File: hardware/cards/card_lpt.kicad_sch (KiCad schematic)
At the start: 20 parts, among them J1 DB25_Pins, U1 74HCT374, U10 74HCT32, U11 74HCT32, U2 74HCT374, U3 74HCT244, U4 74HCT245, U5 74HCT244, U6 74HCT138, U7 74HCT08, U8 74HCT08, U9 74HCT04

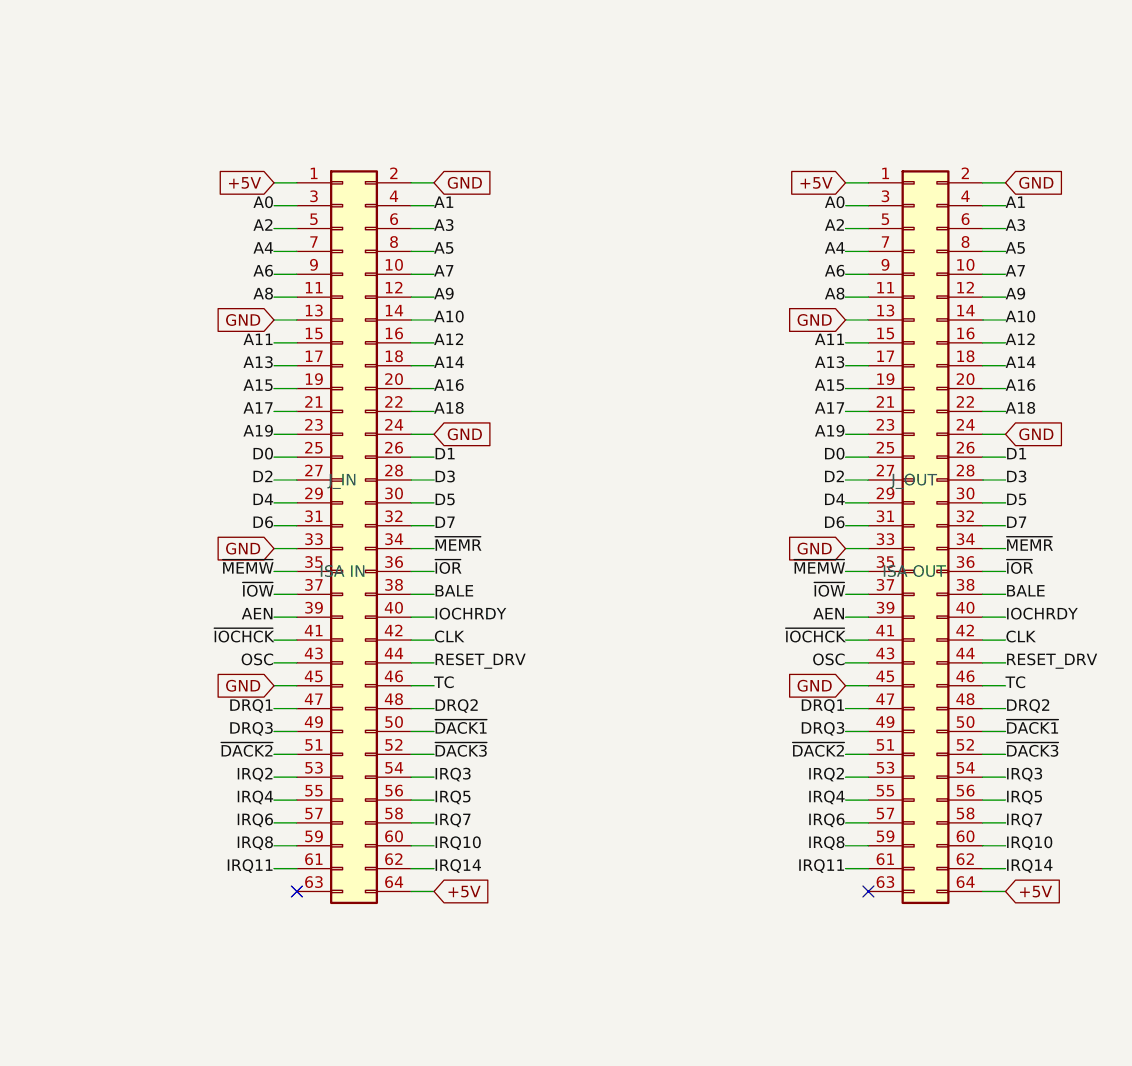
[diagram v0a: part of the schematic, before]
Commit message: Re-base ISA connector on standard 8-bit ISA pinout (60-pin, PicoGUS-style)
isa_conn now uses the standard 8-bit ISA edge pinout on a 60-pin 2.54mm header
(Conn_02x30_Odd_Even), matching the PicoGUS Bus_ISA_8bit layout so the sidecar and
dev cards are pin-compatible with real ISA cards (and 60-pin ribbon is easy to
source). The unused ISA analog rails are reclaimed: pin7 -5V->~{IOCHCK}, pin11
-12V->GND (extra return), pin15 +12V->IRQ8; pin13 reserved/0WS# left NC. Drops the
non-standard IRQ10/11/14 (16-bit-extension signals on a real AT); DACK0/REFRESH#
now on its standard pin (undriven, for card compatibility). Change is confined to
isa_conn.py; sidecar + all card_* sheets inherit it. Verified pin map and
connectivity (IOCHCK->Bus MCU, IRQ8->collector+RTC); zero structural ERC on
motherboard and all five cards.

Co-Authored-By: Claude Opus 4.8 (1M context) <noreply@anthropic.com>
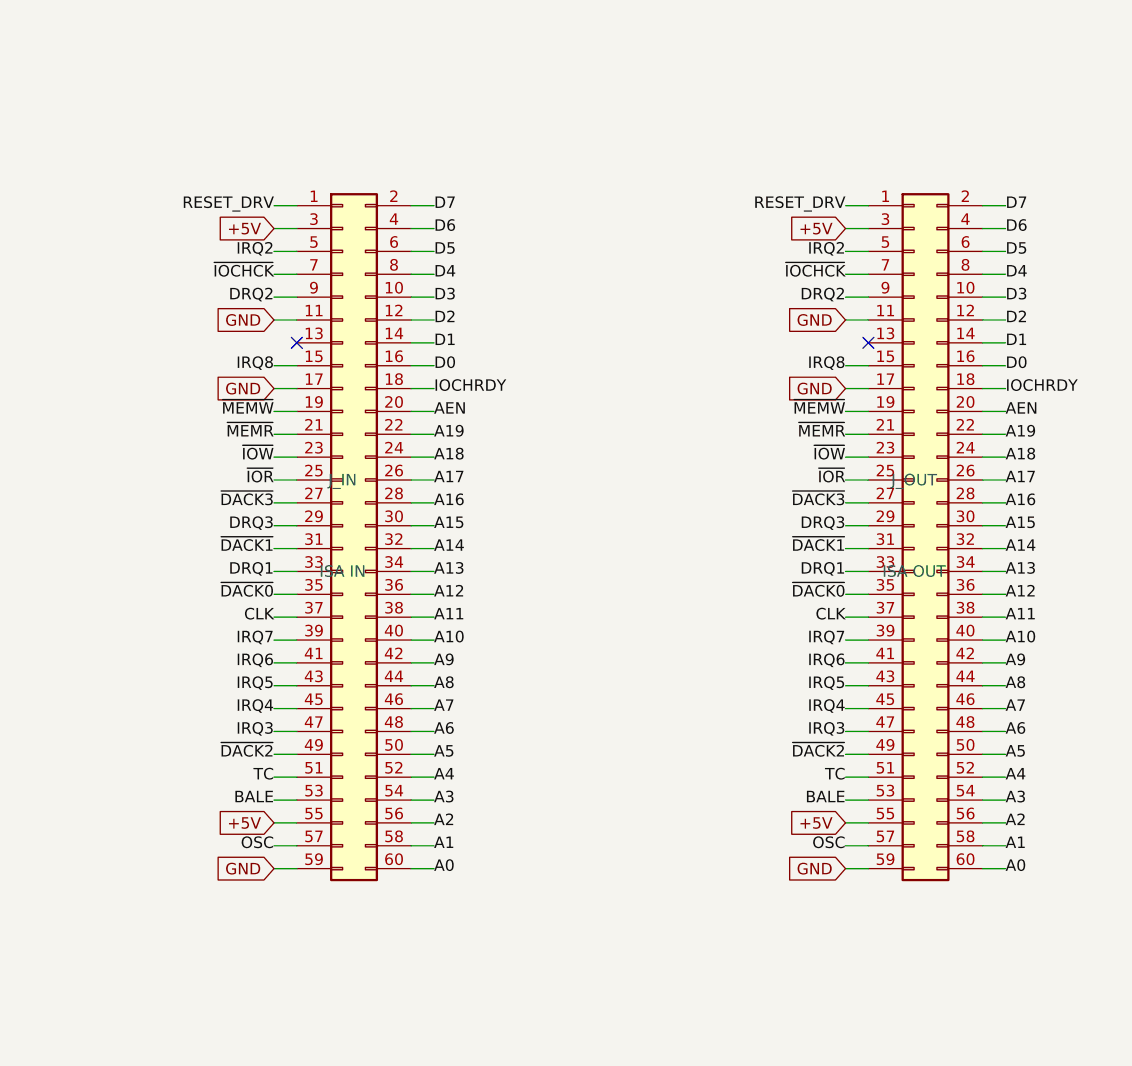
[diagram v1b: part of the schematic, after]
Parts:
- removed J_IN: ISA IN, symbol Connector_Generic:Conn_02x32_Odd_Even
- removed J_OUT: ISA OUT, symbol Connector_Generic:Conn_02x32_Odd_Even
- added J_IN: ISA IN, symbol Connector_Generic:Conn_02x30_Odd_Even
- added J_OUT: ISA OUT, symbol Connector_Generic:Conn_02x30_Odd_Even
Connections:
- net +5V: now also J_IN.3 (Pin_3), J_IN.55 (Pin_55), J_OUT.3 (Pin_3), J_OUT.55 (Pin_55)
- net A0: now also J_IN.60 (Pin_60), J_OUT.60 (Pin_60)
- net A1: now also J_IN.58 (Pin_58), J_OUT.58 (Pin_58)
- net A10: now also J_IN.40 (Pin_40), J_OUT.40 (Pin_40)
- net A11: now also J_IN.38 (Pin_38), J_OUT.38 (Pin_38)
- net A12: now also J_IN.36 (Pin_36), J_OUT.36 (Pin_36)
- net A13: now also J_IN.34 (Pin_34), J_OUT.34 (Pin_34)
- net A14: now also J_IN.32 (Pin_32), J_OUT.32 (Pin_32)
- net A15: now also J_IN.30 (Pin_30), J_OUT.30 (Pin_30)
- net A16: now also J_IN.28 (Pin_28), J_OUT.28 (Pin_28)
- net A17: now also J_IN.26 (Pin_26), J_OUT.26 (Pin_26)
- net A18: now also J_IN.24 (Pin_24), J_OUT.24 (Pin_24)
- net A19: now also J_IN.22 (Pin_22), J_OUT.22 (Pin_22)
- net A2: now also J_IN.56 (Pin_56), J_OUT.56 (Pin_56)
- net A3: now also J_IN.54 (Pin_54), J_OUT.54 (Pin_54)
- net A4: now also J_IN.52 (Pin_52), J_OUT.52 (Pin_52)
- net A5: now also J_IN.50 (Pin_50), J_OUT.50 (Pin_50)
- net A6: now also J_IN.48 (Pin_48), J_OUT.48 (Pin_48)
- net A7: now also J_IN.46 (Pin_46), J_OUT.46 (Pin_46)
- net A8: now also J_IN.44 (Pin_44), J_OUT.44 (Pin_44)
- net A9: now also J_IN.42 (Pin_42), J_OUT.42 (Pin_42)
- net AEN: now also J_IN.20 (Pin_20), J_OUT.20 (Pin_20)
- net BALE: now also J_IN.53 (Pin_53), J_OUT.53 (Pin_53)
- net CLK: now also J_IN.37 (Pin_37), J_OUT.37 (Pin_37)
- net D0: now also J_IN.16 (Pin_16), J_OUT.16 (Pin_16)
- net D1: now also J_IN.14 (Pin_14), J_OUT.14 (Pin_14)
- net D2: now also J_IN.12 (Pin_12), J_OUT.12 (Pin_12)
- net D3: now also J_IN.10 (Pin_10), J_OUT.10 (Pin_10)
- net D4: now also J_IN.8 (Pin_8), J_OUT.8 (Pin_8)
- net D5: now also J_IN.6 (Pin_6), J_OUT.6 (Pin_6)
- net D6: now also J_IN.4 (Pin_4), J_OUT.4 (Pin_4)
- net D7: now also J_IN.2 (Pin_2), J_OUT.2 (Pin_2)
- net DRQ1: now also J_IN.33 (Pin_33), J_OUT.33 (Pin_33)
- net DRQ2: now also J_IN.9 (Pin_9), J_OUT.9 (Pin_9)
- net DRQ3: now also J_IN.29 (Pin_29), J_OUT.29 (Pin_29)
- net GND: now also J_IN.11 (Pin_11), J_IN.17 (Pin_17), J_IN.59 (Pin_59), J_OUT.11 (Pin_11), J_OUT.17 (Pin_17), J_OUT.59 (Pin_59)
- net IOCHRDY: now also J_IN.18 (Pin_18), J_OUT.18 (Pin_18)
- net IRQ2: now also J_IN.5 (Pin_5), J_OUT.5 (Pin_5)
- net IRQ3: now also J_IN.47 (Pin_47), J_OUT.47 (Pin_47)
- net IRQ4: now also J_IN.45 (Pin_45), J_OUT.45 (Pin_45)
- net IRQ5: now also J_IN.43 (Pin_43), J_OUT.43 (Pin_43)
- net IRQ6: now also J_IN.41 (Pin_41), J_OUT.41 (Pin_41)
- net IRQ7: now also J_IN.39 (Pin_39), J_OUT.39 (Pin_39)
- net IRQ8: now also J_IN.15 (Pin_15), J_OUT.15 (Pin_15)
- net OSC: now also J_IN.57 (Pin_57), J_OUT.57 (Pin_57)
- net RESET_DRV: now also J_IN.1 (Pin_1), J_OUT.1 (Pin_1)
- net TC: now also J_IN.51 (Pin_51), J_OUT.51 (Pin_51)
- net ~{DACK1}: now also J_IN.31 (Pin_31), J_OUT.31 (Pin_31)
- net ~{DACK2}: now also J_IN.49 (Pin_49), J_OUT.49 (Pin_49)
- net ~{DACK3}: now also J_IN.27 (Pin_27), J_OUT.27 (Pin_27)
- net ~{IOCHCK}: now also J_IN.7 (Pin_7), J_OUT.7 (Pin_7)
- net ~{IOR}: now also J_IN.25 (Pin_25), J_OUT.25 (Pin_25)
- net ~{IOW}: now also J_IN.23 (Pin_23), J_OUT.23 (Pin_23)
- net ~{MEMR}: now also J_IN.21 (Pin_21), J_OUT.21 (Pin_21)
- net ~{MEMW}: now also J_IN.19 (Pin_19), J_OUT.19 (Pin_19)
- new net ~{DACK0}: J_IN.35 (Pin_35), J_OUT.35 (Pin_35)

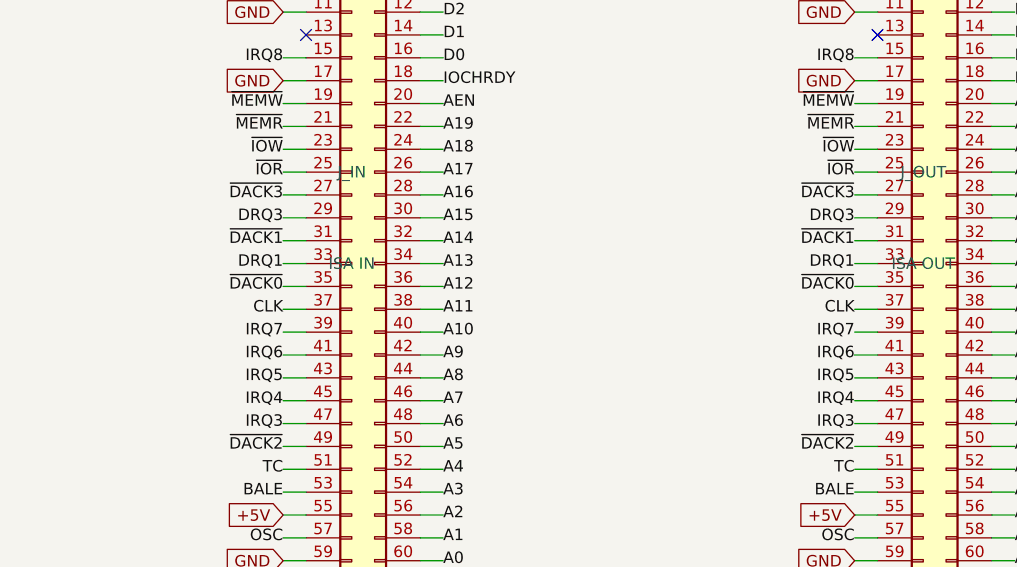
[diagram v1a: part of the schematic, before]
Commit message: Drive ISA REFRESH# from the Bus MCU for DRAM-based cards
Pin 35 (DACK0/REFRESH#) net renamed ~{DACK0} -> ~{REFRESH} in isa_conn and is now
an active Bus MCU output (GPIO47, reclaimed from the redundant raw-~WR sense -- the
MCU tracks writes via the gated MEMW/IOW). Driven from the internal ~15us refresh
timer (same source as the 0x61-bit-4 toggle); a refresh cycle reuses the bus-master
engine to walk the row address on A0-A7 + pulse MEMR#, so DRAM ISA cards see a
standard refresh. ~{REFRESH} added to the Bus MCU interface. Verified it ties
sidecar<->Bus MCU and passes through J_IN<->J_OUT on every dev card; zero
structural ERC on motherboard and all five cards.

Co-Authored-By: Claude Opus 4.8 (1M context) <noreply@anthropic.com>
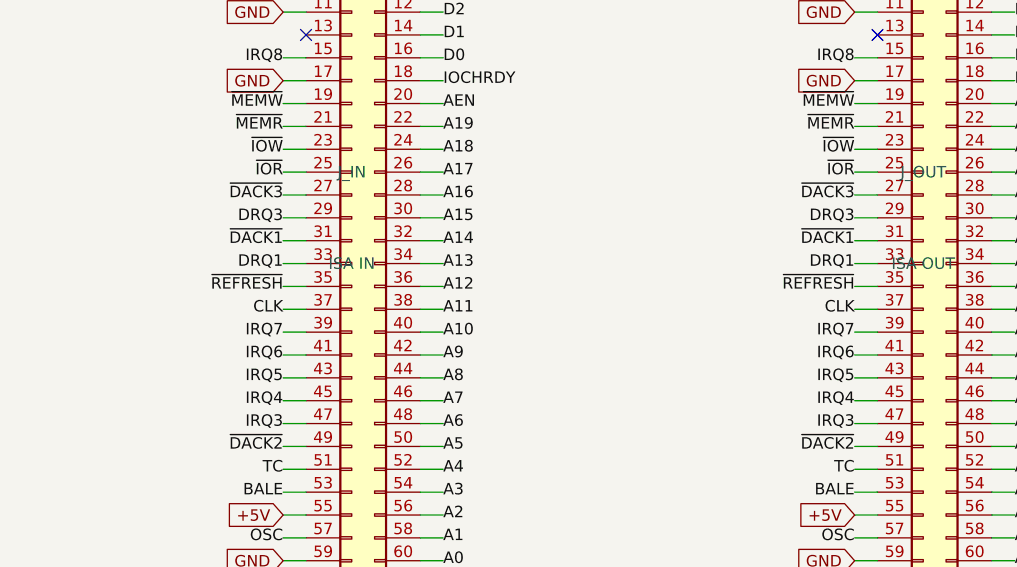
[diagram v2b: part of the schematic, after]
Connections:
- net ~{DACK0} renamed ~{REFRESH}
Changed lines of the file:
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@@
 		)
 	)
-	(label "~{DACK0}"
+	(label "~{REFRESH}"
 		(at 436.88 160.02 180)
 		(effects
@@
 		)
 	)
-	(label "~{DACK0}"
+	(label "~{REFRESH}"
 		(at 500.38 160.02 180)
 		(effects
@@
 		(instances
 			(project "card_lpt"
-				(path "/6a3e43c0-a07d-481b-9625-a33615572297"
+				(path "/3601480a-62b4-4d7d-acc2-271a667b1cb5"
 					(reference "J_IN")
 					(unit 1)
@@
 		(instances
 			(project "card_lpt"
-				(path "/6a3e43c0-a07d-481b-9625-a33615572297"
+				(path "/3601480a-62b4-4d7d-acc2-271a667b1cb5"
 					(reference "J_OUT")
 					(unit 1)
@@
 		(instances
 			(project "card_lpt"
-				(path "/6a3e43c0-a07d-481b-9625-a33615572297"
+				(path "/3601480a-62b4-4d7d-acc2-271a667b1cb5"
 					(reference "U7")
 					(unit 1)
@@
 		(instances
 			(project "card_lpt"
-				(path "/6a3e43c0-a07d-481b-9625-a33615572297"
+				(path "/3601480a-62b4-4d7d-acc2-271a667b1cb5"
 					(reference "U8")
 					(unit 1)
@@
 		(instances
 			(project "card_lpt"
-				(path "/6a3e43c0-a07d-481b-9625-a33615572297"
+				(path "/3601480a-62b4-4d7d-acc2-271a667b1cb5"
 					(reference "U9")
 					(unit 1)
@@
 		(instances
 			(project "card_lpt"
-				(path "/6a3e43c0-a07d-481b-9625-a33615572297"
+				(path "/3601480a-62b4-4d7d-acc2-271a667b1cb5"
 					(reference "U6")
 					(unit 1)
@@
 		(instances
 			(project "card_lpt"
-				(path "/6a3e43c0-a07d-481b-9625-a33615572297"
+				(path "/3601480a-62b4-4d7d-acc2-271a667b1cb5"
 					(reference "U10")
 					(unit 1)
@@
 		(instances
 			(project "card_lpt"
-				(path "/6a3e43c0-a07d-481b-9625-a33615572297"
+				(path "/3601480a-62b4-4d7d-acc2-271a667b1cb5"
 					(reference "U11")
 					(unit 1)
@@
 		(instances
 			(project "card_lpt"
-				(path "/6a3e43c0-a07d-481b-9625-a33615572297"
+				(path "/3601480a-62b4-4d7d-acc2-271a667b1cb5"
 					(reference "U1")
 					(unit 1)
@@
 		(instances
 			(project "card_lpt"
-				(path "/6a3e43c0-a07d-481b-9625-a33615572297"
+				(path "/3601480a-62b4-4d7d-acc2-271a667b1cb5"
 					(reference "U4")
 					(unit 1)
@@
 		(instances
 			(project "card_lpt"
-				(path "/6a3e43c0-a07d-481b-9625-a33615572297"
+				(path "/3601480a-62b4-4d7d-acc2-271a667b1cb5"
 					(reference "U2")
 					(unit 1)
@@
 		(instances
 			(project "card_lpt"
-				(path "/6a3e43c0-a07d-481b-9625-a33615572297"
+				(path "/3601480a-62b4-4d7d-acc2-271a667b1cb5"
 					(reference "U5")
 					(unit 1)
@@
 		(instances
 			(project "card_lpt"
-				(path "/6a3e43c0-a07d-481b-9625-a33615572297"
+				(path "/3601480a-62b4-4d7d-acc2-271a667b1cb5"
 					(reference "U3")
 					(unit 1)
@@
 		(instances
 			(project "card_lpt"
-				(path "/6a3e43c0-a07d-481b-9625-a33615572297"
+				(path "/3601480a-62b4-4d7d-acc2-271a667b1cb5"
 					(reference "J1")
 					(unit 1)
@@
 		(instances
 			(project "card_lpt"
-				(path "/6a3e43c0-a07d-481b-9625-a33615572297"
+				(path "/3601480a-62b4-4d7d-acc2-271a667b1cb5"
 					(reference "C1")
 					(unit 1)
@@
 		(instances
 			(project "card_lpt"
-				(path "/6a3e43c0-a07d-481b-9625-a33615572297"
+				(path "/3601480a-62b4-4d7d-acc2-271a667b1cb5"
 					(reference "C2")
 					(unit 1)
@@
 		(instances
 			(project "card_lpt"
-				(path "/6a3e43c0-a07d-481b-9625-a33615572297"
+				(path "/3601480a-62b4-4d7d-acc2-271a667b1cb5"
 					(reference "C3")
 					(unit 1)
@@
 		(instances
 			(project "card_lpt"
-				(path "/6a3e43c0-a07d-481b-9625-a33615572297"
+				(path "/3601480a-62b4-4d7d-acc2-271a667b1cb5"
 					(reference "C4")
 					(unit 1)
@@
 		(instances
 			(project "card_lpt"
-				(path "/6a3e43c0-a07d-481b-9625-a33615572297"
+				(path "/3601480a-62b4-4d7d-acc2-271a667b1cb5"
 					(reference "C5")
 					(unit 1)
@@
 		(instances
 			(project "card_lpt"
-				(path "/6a3e43c0-a07d-481b-9625-a33615572297"
+				(path "/3601480a-62b4-4d7d-acc2-271a667b1cb5"
 					(reference "C6")
 					(unit 1)

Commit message: Fix all critical+high design-review findings (C1-C5, H1-H8)
Full review in hardware/notes/design-review-2026-07-03.md (with per-item
fix logs). Highlights:
- SRAM strobed by gated MEMR/MEMW (was raw ~RD/~WR: I/O cycles corrupted
  SRAM and the boot shadow-load could never write it)
- Reset chain implemented: NAND combine of ~PWRGOOD + ~CPURESET drives
  V20 RESET and an always-driven RESET_DRV (dropped from the Bus MCU)
- Contention-free bus handoff: '573 OE=HLDA vs counter '244 stage
  ~OE=~HLDA; strobe gates wired + tri-stated ('125, ~OE=HLDA); Bus MCU
  address group fixed to sense; AEN/TC fixed drive; BALE input-only
- '573 LE driven by BALE (was a dangling BALE_L label)
- Data '245 DIR=DT/~R, ~OE=DEN so INTA vectors reach the CPU
- Idle pulls: strobes/DEN high, AEN/IRQ2-9/DRQ low, IOCHRDY/IOCHCK/
  DACK2-3 high
- CH224K CFG1 left open (grounding it selects 9-20V, not 5V)
- XT-IDE INTRQ pull-down (pull-up parked IRQ5 asserted)
- LPT status bit7 = ~Busy via spare inverter (SPP semantics)
- Audio summer TL072 -> MCP6002 (RRIO; TL072 out of spec at +5V single
  supply)
- card_isatest: DUT P-FET gate to V5RAW + NPN driver (default off, can
  fully turn off); /3 divider TC->~PE reload actually wired

Overturned picks corrected in notes/questions-*.md. All sheets + cards
rebuilt; structural ERC = 0; fixes netlist-verified.

Co-Authored-By: Claude Fable 5 <noreply@anthropic.com>
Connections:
- net GND: no longer U9.13 (P13)
- net P_BUSY: now also U9.13 (P13); no longer U3.2 (1A0)
- net BUSY_N: now reaches U9.12 (P12)
- net BUSY_N: now also U3.2 (1A0)
- no-connect marks 18 -> 17
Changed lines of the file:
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@@
 		)
 	)
-	(global_label "GND"
-		(shape input)
+	(label "P_BUSY"
 		(at 59.69 184.15 180)
 		(effects
@@
 		)
 	)
-	(no_connect
-		(at 90.17 184.15)
+	(wire
+		(pts
+			(xy 90.17 184.15)
+			(xy 92.71 184.15)
+		)
+		(stroke
+			(width 0)
+			(type default)
+		)
+	)
+	(label "BUSY_N"
+		(at 92.71 184.15 0)
+		(effects
+			(font
+				(size 1.27 1.27)
+			)
+		)
 	)
 	(wire
@@
 		)
 	)
-	(label "P_BUSY"
+	(label "BUSY_N"
 		(at 186.69 217.17 180)
 		(effects
@@
 		(instances
 			(project "card_lpt"
-				(path "/d0d6c778-9dee-4e65-88c1-90d9ddd9256b"
+				(path "/4e3f5f18-a6f2-4a5e-a60d-ceab254b2380"
 					(reference "J_IN")
 					(unit 1)
@@
 		(instances
 			(project "card_lpt"
-				(path "/d0d6c778-9dee-4e65-88c1-90d9ddd9256b"
+				(path "/4e3f5f18-a6f2-4a5e-a60d-ceab254b2380"
 					(reference "J_OUT")
 					(unit 1)
@@
 		(instances
 			(project "card_lpt"
-				(path "/d0d6c778-9dee-4e65-88c1-90d9ddd9256b"
+				(path "/4e3f5f18-a6f2-4a5e-a60d-ceab254b2380"
 					(reference "U7")
 					(unit 1)
@@
 		(instances
 			(project "card_lpt"
-				(path "/d0d6c778-9dee-4e65-88c1-90d9ddd9256b"
+				(path "/4e3f5f18-a6f2-4a5e-a60d-ceab254b2380"
 					(reference "U8")
 					(unit 1)
@@
 		(instances
 			(project "card_lpt"
-				(path "/d0d6c778-9dee-4e65-88c1-90d9ddd9256b"
+				(path "/4e3f5f18-a6f2-4a5e-a60d-ceab254b2380"
 					(reference "U9")
 					(unit 1)
@@
 		(instances
 			(project "card_lpt"
-				(path "/d0d6c778-9dee-4e65-88c1-90d9ddd9256b"
+				(path "/4e3f5f18-a6f2-4a5e-a60d-ceab254b2380"
 					(reference "U6")
 					(unit 1)
@@
 		(instances
 			(project "card_lpt"
-				(path "/d0d6c778-9dee-4e65-88c1-90d9ddd9256b"
+				(path "/4e3f5f18-a6f2-4a5e-a60d-ceab254b2380"
 					(reference "U10")
 					(unit 1)
@@
 		(instances
 			(project "card_lpt"
-				(path "/d0d6c778-9dee-4e65-88c1-90d9ddd9256b"
+				(path "/4e3f5f18-a6f2-4a5e-a60d-ceab254b2380"
 					(reference "U11")
 					(unit 1)
@@
 		(instances
 			(project "card_lpt"
-				(path "/d0d6c778-9dee-4e65-88c1-90d9ddd9256b"
+				(path "/4e3f5f18-a6f2-4a5e-a60d-ceab254b2380"
 					(reference "U1")
 					(unit 1)
@@
 		(instances
 			(project "card_lpt"
-				(path "/d0d6c778-9dee-4e65-88c1-90d9ddd9256b"
+				(path "/4e3f5f18-a6f2-4a5e-a60d-ceab254b2380"
 					(reference "U4")
 					(unit 1)
@@
 		(instances
 			(project "card_lpt"
-				(path "/d0d6c778-9dee-4e65-88c1-90d9ddd9256b"
+				(path "/4e3f5f18-a6f2-4a5e-a60d-ceab254b2380"
 					(reference "U2")
 					(unit 1)
@@
 		(instances
 			(project "card_lpt"
-				(path "/d0d6c778-9dee-4e65-88c1-90d9ddd9256b"
+				(path "/4e3f5f18-a6f2-4a5e-a60d-ceab254b2380"
 					(reference "U5")
 					(unit 1)
@@
 		(instances
 			(project "card_lpt"
-				(path "/d0d6c778-9dee-4e65-88c1-90d9ddd9256b"
+				(path "/4e3f5f18-a6f2-4a5e-a60d-ceab254b2380"
 					(reference "U3")
 					(unit 1)
@@
 		(instances
 			(project "card_lpt"
-				(path "/d0d6c778-9dee-4e65-88c1-90d9ddd9256b"
+				(path "/4e3f5f18-a6f2-4a5e-a60d-ceab254b2380"
 					(reference "J1")
 					(unit 1)
@@
 		(instances
 			(project "card_lpt"
-				(path "/d0d6c778-9dee-4e65-88c1-90d9ddd9256b"
+				(path "/4e3f5f18-a6f2-4a5e-a60d-ceab254b2380"
 					(reference "C1")
 					(unit 1)
@@
 		(instances
 			(project "card_lpt"
-				(path "/d0d6c778-9dee-4e65-88c1-90d9ddd9256b"
+				(path "/4e3f5f18-a6f2-4a5e-a60d-ceab254b2380"
 					(reference "C2")
 					(unit 1)
@@
 		(instances
 			(project "card_lpt"
-				(path "/d0d6c778-9dee-4e65-88c1-90d9ddd9256b"
+				(path "/4e3f5f18-a6f2-4a5e-a60d-ceab254b2380"
 					(reference "C3")
 					(unit 1)
@@
 		(instances
 			(project "card_lpt"
-				(path "/d0d6c778-9dee-4e65-88c1-90d9ddd9256b"
+				(path "/4e3f5f18-a6f2-4a5e-a60d-ceab254b2380"
 					(reference "C4")
 					(unit 1)
@@
 		(instances
 			(project "card_lpt"
-				(path "/d0d6c778-9dee-4e65-88c1-90d9ddd9256b"
+				(path "/4e3f5f18-a6f2-4a5e-a60d-ceab254b2380"
 					(reference "C5")
 					(unit 1)
@@
 		(instances
 			(project "card_lpt"
-				(path "/d0d6c778-9dee-4e65-88c1-90d9ddd9256b"
+				(path "/4e3f5f18-a6f2-4a5e-a60d-ceab254b2380"
 					(reference "C6")
 					(unit 1)
